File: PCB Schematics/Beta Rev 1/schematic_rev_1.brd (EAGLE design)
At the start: 100 x 80 mm, 10 parts, among them IC1 STM8S003F3

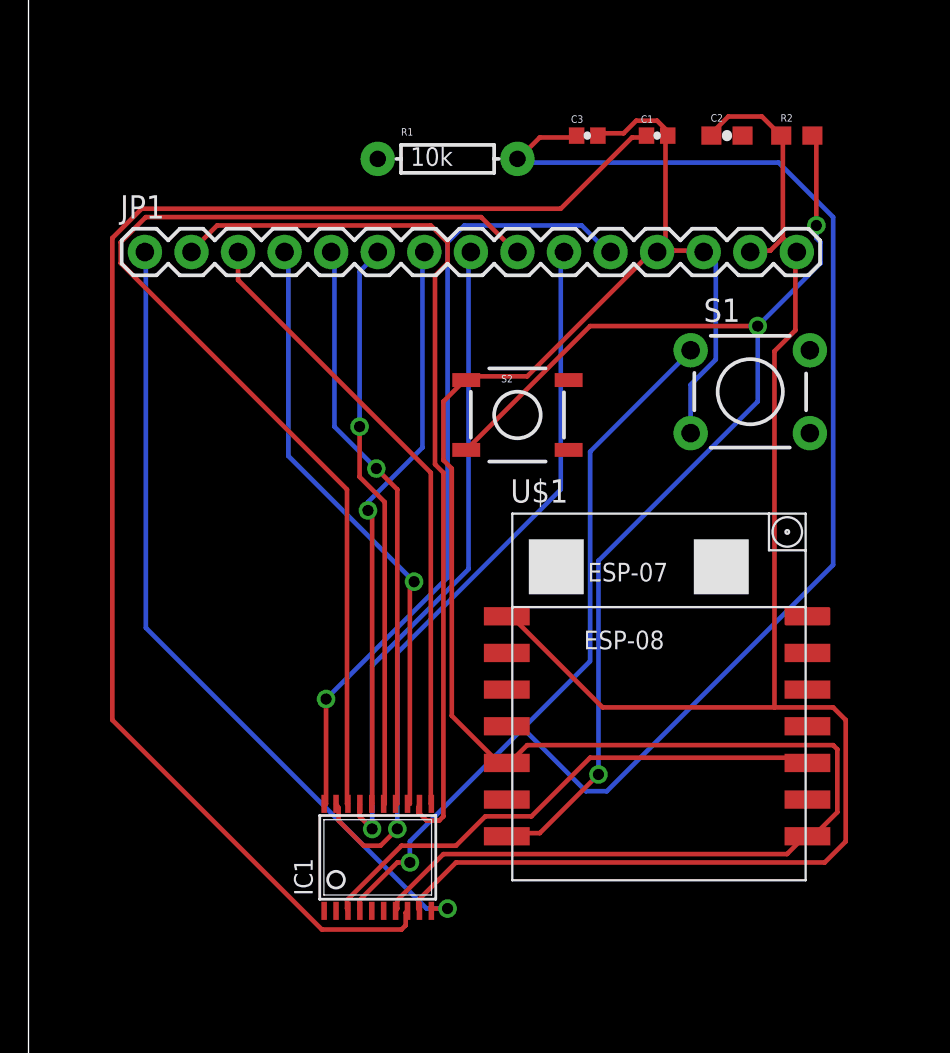
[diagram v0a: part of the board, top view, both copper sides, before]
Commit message: Updated schematic by Manivannan. Corrected component placements and cleaned up the nets.
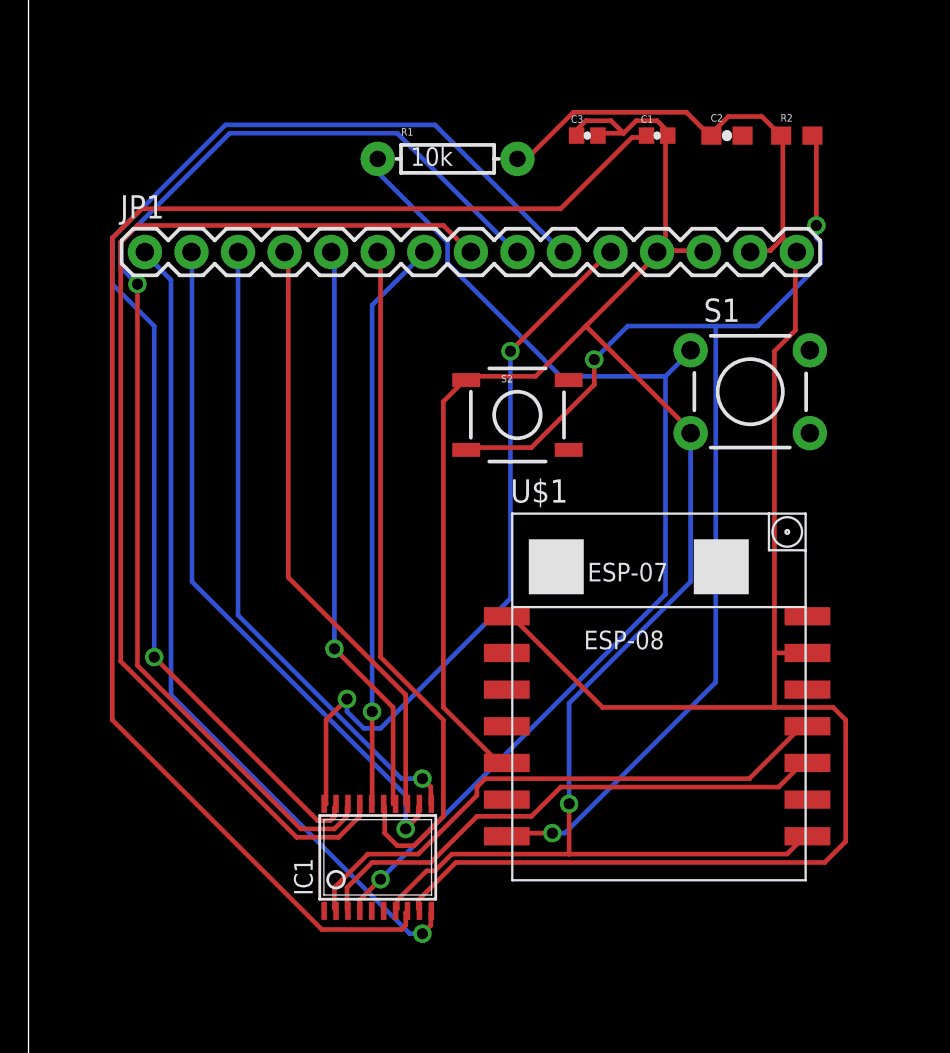
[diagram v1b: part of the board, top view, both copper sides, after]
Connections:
- removed net N$2: IC1.2
- removed net N$7 (its old number): IC1.1
- new net N$18: C3.2, IC1.4, R1.P$1, S1.1
- new net N$5: IC1.2, U$1.RX
- net +3V3: now also R1.P$2, U$1.CH_PD; no longer U$1.VCC
- net GND: now also C3.1; no longer C3.2
- net N$4: now also U$1.GPIO16; no longer C3.1, IC1.4, R1.P$2, S1.1
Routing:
- net N$4: track 103.2 -> 0.00 mm, vias 1 -> 0
- net N$18: track 0.00 -> 59.8 mm, vias 0 -> 1
- net N$5: track 0.00 -> 31.1 mm
- net N$16: track 40.3 -> 68.2 mm
- net N$14: track 35.3 -> 61.1 mm, vias 1 -> 0
- net +3V3: track 91.6 -> 105.3 mm
- net N$8: track 48.9 -> 38.0 mm, vias 0 -> 1
- net N$15: track 58.8 -> 66.3 mm, vias 0 -> 1
- net N$12: track 31.1 -> 38.0 mm, vias 1 -> 0
- net N$17: track 43.3 -> 40.4 mm, vias 1 -> 2
- net GND: track 110.3 -> 111.8 mm, vias 0 -> 1
- net N$6: track 44.4 -> 45.3 mm
- net N$9: track 34.5 -> 35.2 mm, vias 0 -> 1
- net N$19: track 65.2 -> 65.8 mm
- net N$10: track 33.3 -> 33.0 mm, vias 1 -> 0
